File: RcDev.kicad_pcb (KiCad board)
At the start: 2 copper layers, 45.5 x 29.1 mm, 38 parts, among them J1 Thro CH4, J10 VBatt, J2 Ruddr CH3, J3 Program, J4 Elev CH2, J5 Aile CH1, J6 Model Power 7V4, J7 USB_B_Mini, J8 Batt1 3V7, J9 Batt2 3V7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

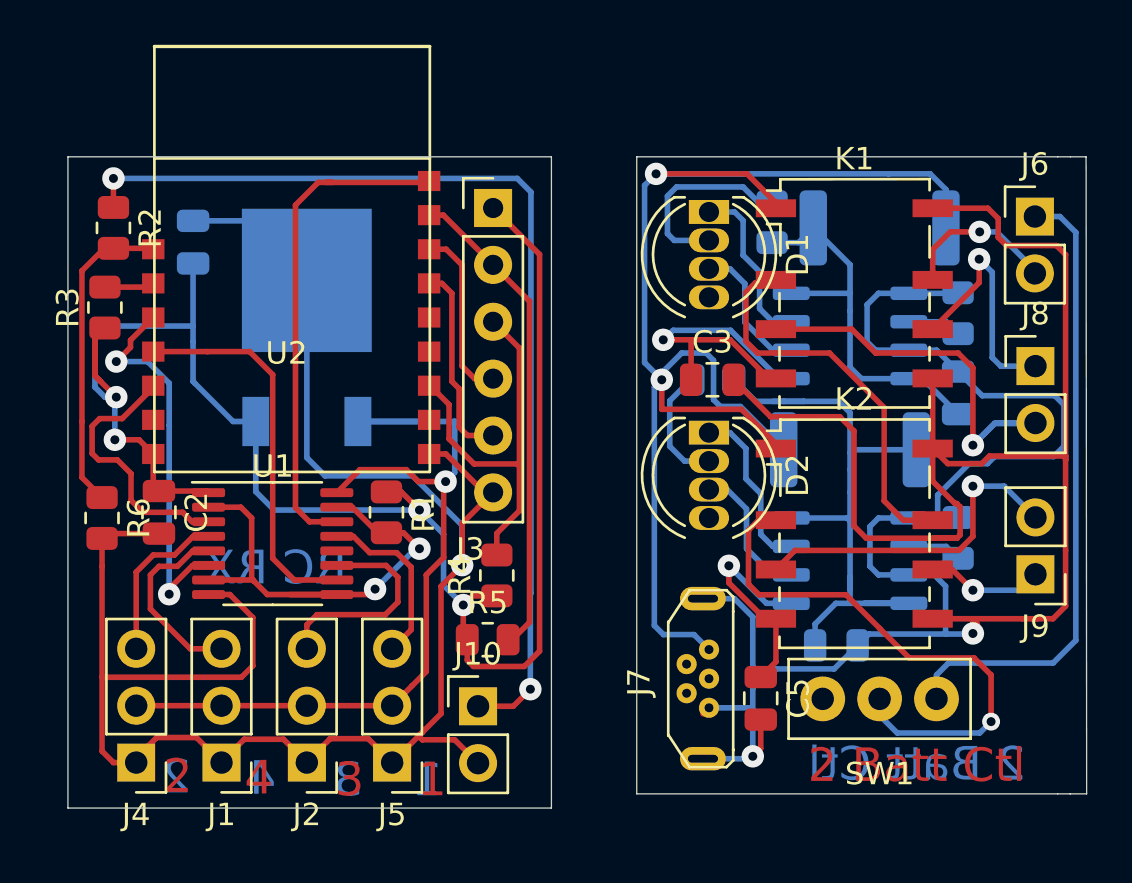
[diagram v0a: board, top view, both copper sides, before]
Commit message: Tweaks to make it more correct to assembly in 3D view (no real change to PCBs)
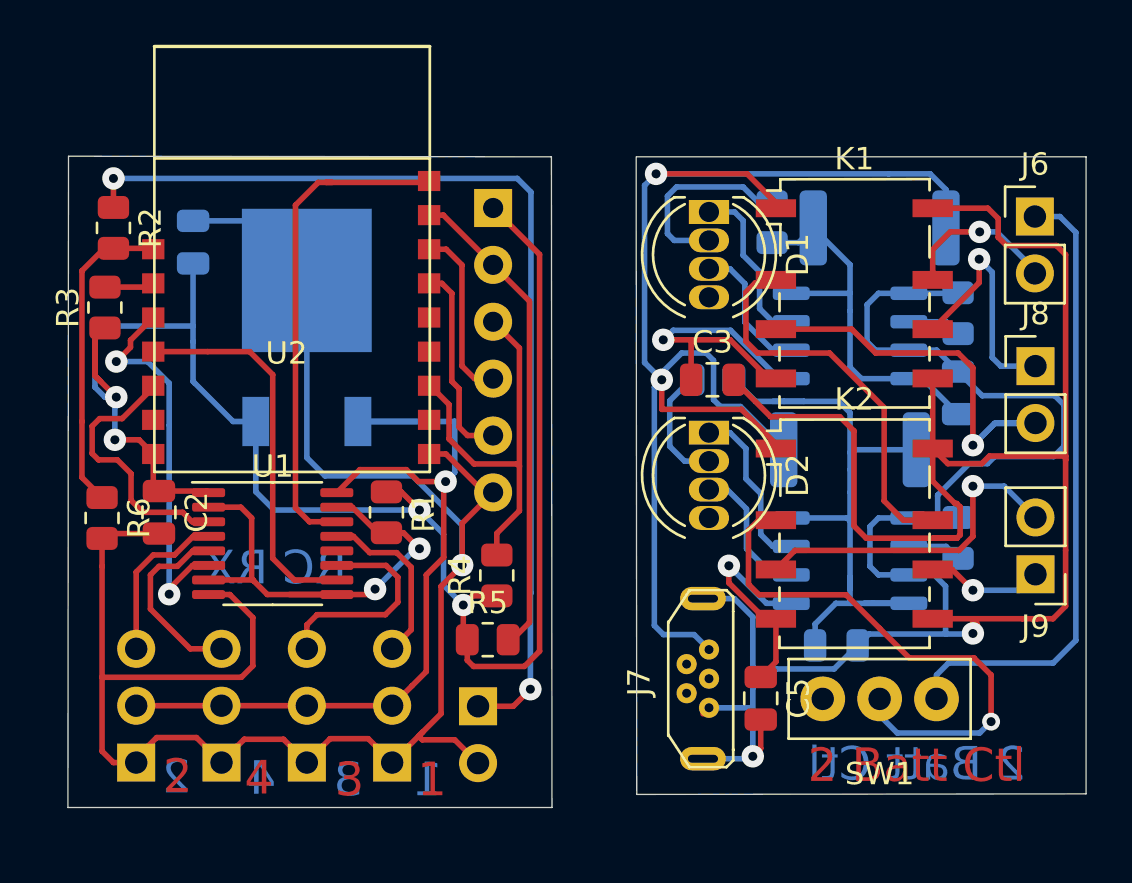
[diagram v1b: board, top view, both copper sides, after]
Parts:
- J1, J10, J2, J4, J5: moved to B.Cu
- J3: footprint TrevM:PinHeader_1x06_P2.54mm_Vertical_bentR -> TrevM:PinHeader_1x06_P2.54mm_Vertical_bent; moved to B.Cu
- turned J1 to 0 degrees
- turned J10 to 180 degrees
- turned J2 to 0 degrees
- turned J3 to 180 degrees
- turned J4 to 0 degrees
- turned J5 to 0 degrees
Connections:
- net Net-(J6-Pad1) renamed /O+
- net Net-(J6-Pad2) renamed /O-
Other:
- outline, holes or cut-outs redrawn

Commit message: Added 100nF capacitor to ADC
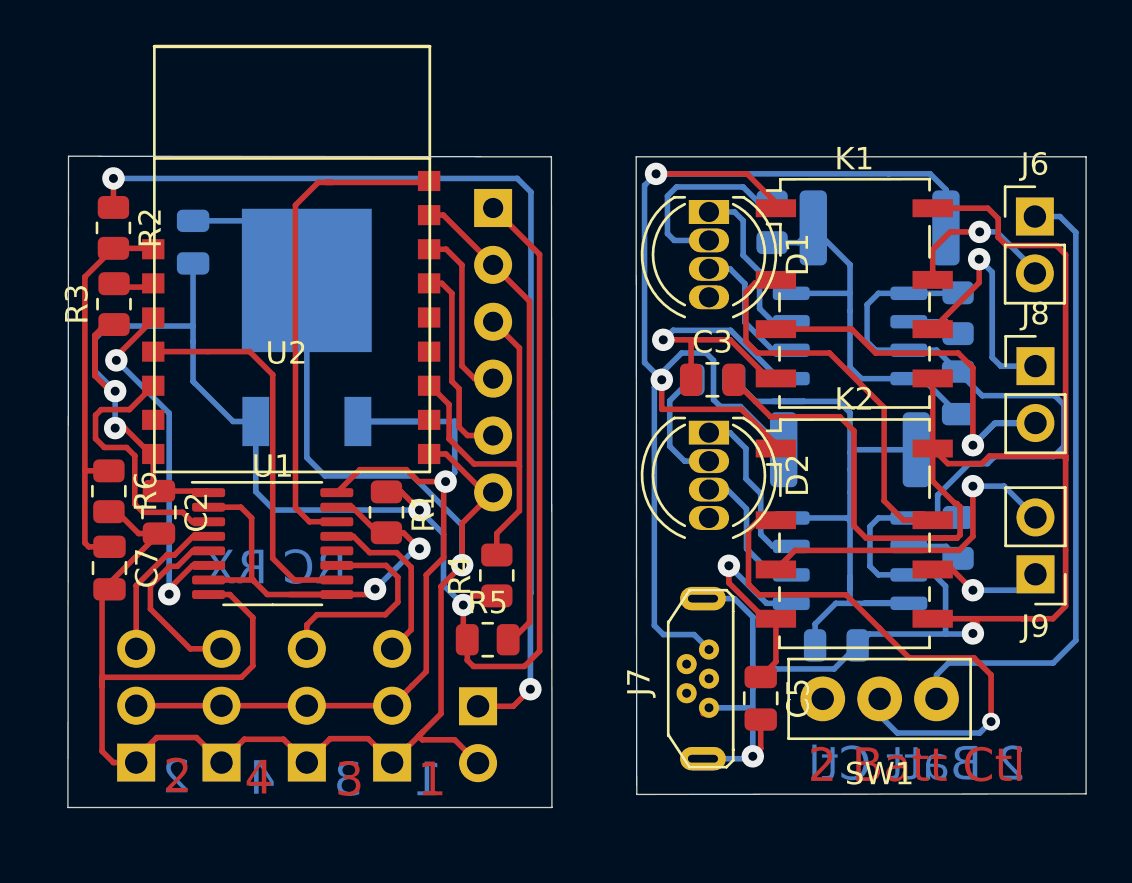
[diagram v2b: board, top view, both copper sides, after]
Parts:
- added C7: 100nF, Capacitor_SMD:C_0805_2012Metric, F.Cu at (107.5, 68.7)
- moved R6 1.23 mm to (107.5, 65.2)
- moved R3 0.43 mm to (107.7, 56.9)
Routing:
- net Net-(C7-Pad1): track 14.3 -> 17.9 mm
- net GND: track 84.8 -> 86.3 mm
- net Net-(U1-Pad6): track 17.6 -> 16.7 mm
- net +3V3: track 77.5 -> 76.6 mm

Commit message: Tidy up silk screens
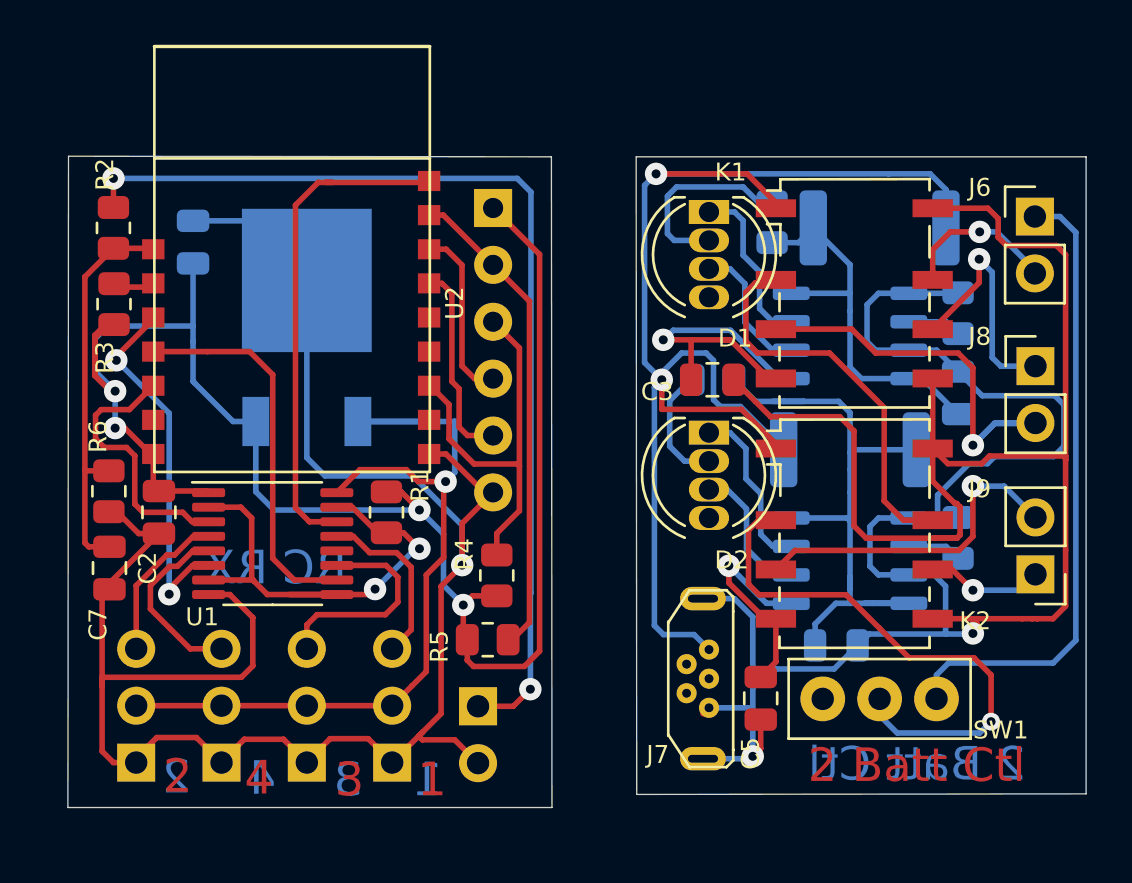
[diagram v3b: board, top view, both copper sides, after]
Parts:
- C1, C3, C4, C5, C6: value 10uF -> 10u
- C2, C7: value 100nF -> 100n
- D1: value LED_RCGB -> Chg1
- D2: value LED_RCGB -> Chg2
- J6: value Model Power 7V4 -> O/P 7V4
- J7: value USB_B_Mini -> USB
- J8: value Batt1 3V7 -> Batt1
- J9: value Batt2 3V7 -> Batt2
- SW1: value SW_SPST -> On/Off

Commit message: Spacing out
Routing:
- net +BATT: track 38.7 -> 33.9 mm
- net /1+: track 20.0 -> 16.2 mm
- net Net-(C3-Pad1): track 14.5 -> 15.6 mm
- net Net-(U1-Pad6): track 16.7 -> 17.6 mm
- net /1-: track 10.7 -> 11.5 mm
- net GND: track 86.3 -> 85.5 mm
- net Net-(C6-Pad1): track 29.4 -> 30.2 mm
- net Net-(C4-Pad1): track 17.3 -> 18.0 mm
- net +3V3: track 76.6 -> 76.0 mm
- net /CH3: track 9.61 -> 8.99 mm
